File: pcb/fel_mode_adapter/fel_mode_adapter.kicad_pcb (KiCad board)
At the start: 2 copper layers, 16.7 x 16.2 mm, 4 parts, among them J1 USB_A, P1 USB_C_Plug_USB2.0

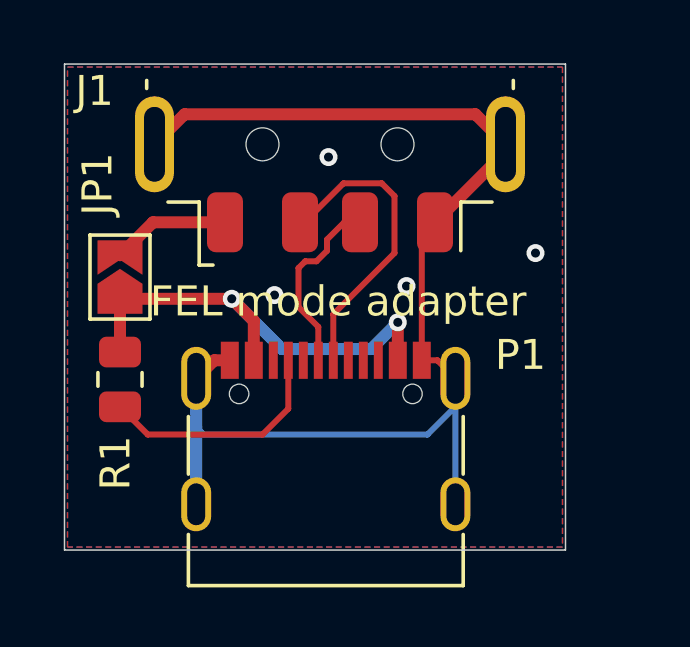
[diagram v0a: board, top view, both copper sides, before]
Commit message: Adds a GND test point to the FEL mode adapter.
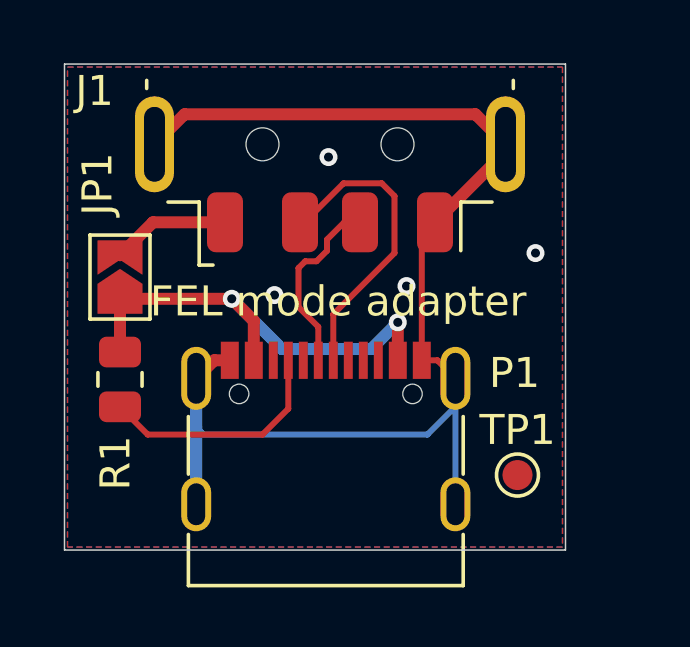
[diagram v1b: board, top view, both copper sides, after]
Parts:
- added TP1: TestPoint, TestPoint:TestPoint_Pad_D1.0mm, F.Cu at (170.5, 90.1)
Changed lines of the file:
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@@
 	(net 6 "Net-(P1-CC)")
 	(net 7 "GND")
+	(footprint "TestPoint:TestPoint_Pad_D1.0mm"
+		(layer "F.Cu")
+		(at 170.5 90.1)
+		(descr "SMD pad as test Point, diameter 1.0mm")
+		(tags "test point SMD pad")
+		(property "Reference" "TP1"
+			(at 0 -1.5 0)
+			(layer "F.SilkS")
+			(effects
+				(font
+					(size 1 1)
+					(thickness 0.15)
+				)
+			)
+		)
+		(property "Value" "TestPoint"
+			(at 0 1.55 0)
+			(layer "F.Fab")
+			(effects
+				(font
+					(size 1 1)
+					(thickness 0.15)
+				)
+			)
+		)
+		(property "Footprint" "TestPoint:TestPoint_Pad_D1.0mm"
+			(at 0 0 0)
+			(unlocked yes)
+			(layer "F.Fab")
+			(hide yes)
+			(effects
+				(font
+					(size 1.27 1.27)
+					(thickness 0.15)
+				)
+			)
+		)
+		(property "Datasheet" ""
+			(at 0 0 0)
+			(unlocked yes)
+			(layer "F.Fab")
+			(hide yes)
+			(effects
+				(font
+					(size 1.27 1.27)
+					(thickness 0.15)
+				)
+			)
+		)
+		(property "Description" "test point"
+			(at 0 0 0)
+			(unlocked yes)
+			(layer "F.Fab")
+			(hide yes)
+			(effects
+				(font
+					(size 1.27 1.27)
+					(thickness 0.15)
+				)
+			)
+		)
+		(property ki_fp_filters "Pin* Test*")
+		(sheetname "Root")
+		(sheetfile "fel_mode_adapter.kicad_sch")
+		(attr exclude_from_pos_files)
+		(fp_circle
+			(center 0 0)
+			(end 0 0.7)
+			(stroke
+				(width 0.12)
+				(type solid)
+			)
+			(fill none)
+			(layer "F.SilkS")
+		)
+		(fp_circle
+			(center 0 0)
+			(end 1 0)
+			(stroke
+				(width 0.05)
+				(type solid)
+			)
+			(fill none)
+			(layer "F.CrtYd")
+		)
+		(fp_text user "${REFERENCE}"
+			(at 0 -1.45 0)
+			(layer "F.Fab")
+			(effects
+				(font
+					(size 1 1)
+					(thickness 0.15)
+				)
+			)
+		)
+		(pad "1" smd circle
+			(at 0 0)
+			(size 1 1)
+			(layers "F.Cu" "F.Mask")
+			(net 7 "GND")
+			(pinfunction "1")
+			(pintype "passive")
+		)
+	)
 	(footprint "Connector_USB:USB_C_Receptacle_G-Switch_GT-USB-7010ASV"
 		(layer "F.Cu")
@@
 		(tags "USB C Type-C Receptacle SMD")
 		(property "Reference" "P1"
-			(at 6.49 -3.9 0)
+			(at 6.29 -3.3 0)
 			(layer "F.SilkS")
 			(effects
@@
 				(font
 					(size 1.27 1.27)
+					(thickness 0.15)
+				)
+			)
+		)
+		(property "farnell" "3777659"
+			(at 0 0 0)
+			(unlocked yes)
+			(layer "F.Fab")
+			(hide yes)
+			(effects
+				(font
+					(size 1 1)
 					(thickness 0.15)
 				)
@@
 			(size 0.65 0.65)
 			(drill 0.65)
-			(layers "*.Cu" "*.Mask")
+			(layers "*.Cu" "*.Mask" "In1.Cu" "In2.Cu" "In3.Cu" "In4.Cu" "In5.Cu" "In6.Cu"
+				"In7.Cu" "In8.Cu" "In9.Cu" "In10.Cu" "In11.Cu" "In12.Cu" "In13.Cu" "In14.Cu"
+				"In15.Cu" "In16.Cu" "In17.Cu" "In18.Cu" "In19.Cu" "In20.Cu" "In21.Cu"
+				"In22.Cu" "In23.Cu" "In24.Cu" "In25.Cu" "In26.Cu" "In27.Cu" "In28.Cu"
+				"In29.Cu" "In30.Cu"
+			)
 		)
 		(pad "" np_thru_hole circle
@@
 			(size 0.65 0.65)
 			(drill 0.65)
-			(layers "*.Cu" "*.Mask")
+			(layers "*.Cu" "*.Mask" "In1.Cu" "In2.Cu" "In3.Cu" "In4.Cu" "In5.Cu" "In6.Cu"
+				"In7.Cu" "In8.Cu" "In9.Cu" "In10.Cu" "In11.Cu" "In12.Cu" "In13.Cu" "In14.Cu"
+				"In15.Cu" "In16.Cu" "In17.Cu" "In18.Cu" "In19.Cu" "In20.Cu" "In21.Cu"
+				"In22.Cu" "In23.Cu" "In24.Cu" "In25.Cu" "In26.Cu" "In27.Cu" "In28.Cu"
+				"In29.Cu" "In30.Cu"
+			)
 		)
 		(pad "A1" smd rect
@@
 			(size 1 2.1)
 			(drill oval 0.6 1.7)
-			(layers "*.Cu" "*.Mask")
+			(layers "*.Cu" "*.Mask" "In1.Cu" "In2.Cu" "In3.Cu" "In4.Cu" "In5.Cu" "In6.Cu"
+				"In7.Cu" "In8.Cu" "In9.Cu" "In10.Cu" "In11.Cu" "In12.Cu" "In13.Cu" "In14.Cu"
+				"In15.Cu" "In16.Cu" "In17.Cu" "In18.Cu" "In19.Cu" "In20.Cu" "In21.Cu"
+				"In22.Cu" "In23.Cu" "In24.Cu" "In25.Cu" "In26.Cu" "In27.Cu" "In28.Cu"
+				"In29.Cu" "In30.Cu"
+			)
 			(remove_unused_layers no)
 			(net 7 "GND")
@@
 			(size 1 1.8)
 			(drill oval 0.6 1.4)
-			(layers "*.Cu" "*.Mask")
+			(layers "*.Cu" "*.Mask" "In1.Cu" "In2.Cu" "In3.Cu" "In4.Cu" "In5.Cu" "In6.Cu"
+				"In7.Cu" "In8.Cu" "In9.Cu" "In10.Cu" "In11.Cu" "In12.Cu" "In13.Cu" "In14.Cu"
+				"In15.Cu" "In16.Cu" "In17.Cu" "In18.Cu" "In19.Cu" "In20.Cu" "In21.Cu"
+				"In22.Cu" "In23.Cu" "In24.Cu" "In25.Cu" "In26.Cu" "In27.Cu" "In28.Cu"
+				"In29.Cu" "In30.Cu"
+			)
 			(remove_unused_layers no)
 			(net 7 "GND")
@@
 			(size 1 2.1)
 			(drill oval 0.6 1.7)
-			(layers "*.Cu" "*.Mask")
+			(layers "*.Cu" "*.Mask" "In1.Cu" "In2.Cu" "In3.Cu" "In4.Cu" "In5.Cu" "In6.Cu"
+				"In7.Cu" "In8.Cu" "In9.Cu" "In10.Cu" "In11.Cu" "In12.Cu" "In13.Cu" "In14.Cu"
+				"In15.Cu" "In16.Cu" "In17.Cu" "In18.Cu" "In19.Cu" "In20.Cu" "In21.Cu"
+				"In22.Cu" "In23.Cu" "In24.Cu" "In25.Cu" "In26.Cu" "In27.Cu" "In28.Cu"
+				"In29.Cu" "In30.Cu"
+			)
 			(remove_unused_layers no)
 			(net 7 "GND")
@@
 			(size 1 1.8)
 			(drill oval 0.6 1.4)
-			(layers "*.Cu" "*.Mask")
+			(layers "*.Cu" "*.Mask" "In1.Cu" "In2.Cu" "In3.Cu" "In4.Cu" "In5.Cu" "In6.Cu"
+				"In7.Cu" "In8.Cu" "In9.Cu" "In10.Cu" "In11.Cu" "In12.Cu" "In13.Cu" "In14.Cu"
+				"In15.Cu" "In16.Cu" "In17.Cu" "In18.Cu" "In19.Cu" "In20.Cu" "In21.Cu"
+				"In22.Cu" "In23.Cu" "In24.Cu" "In25.Cu" "In26.Cu" "In27.Cu" "In28.Cu"
+				"In29.Cu" "In30.Cu"
+			)
 			(remove_unused_layers no)
 			(net 7 "GND")
@@
 			)
 		)
+		(property "farnell" "2313729"
+			(at 0 0 90)
+			(unlocked yes)
+			(layer "F.Fab")
+			(hide yes)
+			(effects
+				(font
+					(size 1 1)
+					(thickness 0.15)
+				)
+			)
+		)
 		(property ki_fp_filters "USB*")
 		(sheetname "Root")
@@
 		)
 		(fp_text user "PCB Edge"
-			(at -6.25 0 360)
+			(at -6.25 0 0)
 			(layer "Dwgs.User")
 			(effects
@@
 			(size 3.2 1.3)
 			(drill oval 2.5 0.7)
-			(layers "*.Cu" "*.Mask")
+			(layers "*.Cu" "*.Mask" "In1.Cu" "In2.Cu" "In3.Cu" "In4.Cu" "In5.Cu" "In6.Cu"
+				"In7.Cu" "In8.Cu" "In9.Cu" "In10.Cu" "In11.Cu" "In12.Cu" "In13.Cu" "In14.Cu"
+				"In15.Cu" "In16.Cu" "In17.Cu" "In18.Cu" "In19.Cu" "In20.Cu" "In21.Cu"
+				"In22.Cu" "In23.Cu" "In24.Cu" "In25.Cu" "In26.Cu" "In27.Cu" "In28.Cu"
+				"In29.Cu" "In30.Cu"
+			)
 			(remove_unused_layers no)
 			(net 7 "GND")
@@
 			(size 3.2 1.3)
 			(drill oval 2.5 0.7)
-			(layers "*.Cu" "*.Mask")
+			(layers "*.Cu" "*.Mask" "In1.Cu" "In2.Cu" "In3.Cu" "In4.Cu" "In5.Cu" "In6.Cu"
+				"In7.Cu" "In8.Cu" "In9.Cu" "In10.Cu" "In11.Cu" "In12.Cu" "In13.Cu" "In14.Cu"
+				"In15.Cu" "In16.Cu" "In17.Cu" "In18.Cu" "In19.Cu" "In20.Cu" "In21.Cu"
+				"In22.Cu" "In23.Cu" "In24.Cu" "In25.Cu" "In26.Cu" "In27.Cu" "In28.Cu"
+				"In29.Cu" "In30.Cu"
+			)
 			(remove_unused_layers no)
 			(net 7 "GND")
@@
 		(net 7)
 		(net_name "GND")
-		(layers "F&B.Cu")
+		(layers "F.Cu" "B.Cu")
 		(hatch edge 0.5)
 		(connect_pads
